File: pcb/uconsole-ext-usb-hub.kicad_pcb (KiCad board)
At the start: 2 copper layers, 32.1 x 77 mm, 38 parts, among them J1 MINI_PCIE, J2 SPEAKER, J3 SPEAKER, P1 USB_C_Plug_USB2.0, P2 USB_C_Plug_USB2.0, P3 USB_C_Plug_USB2.0, P4 USB_C_Plug_USB2.0, U1 TUSB2048B, U2 TPS2044D, U3 USBLC6-2P6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

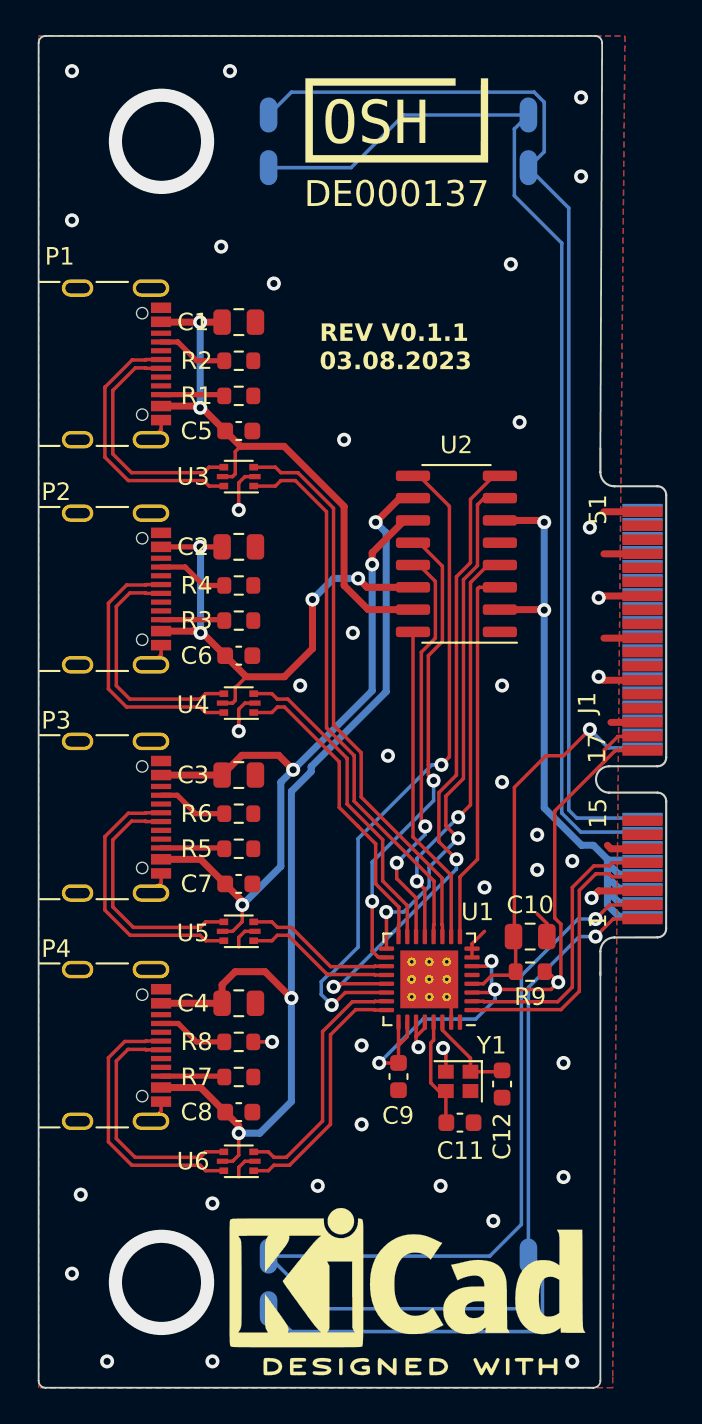
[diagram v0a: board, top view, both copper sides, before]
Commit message: Some updates of sch, pcb and readme
* Add 3 u.fl connectors for antennas
* Update pictures in readme

Signed-off-by: argz <kirill.snezhko@pm.me>
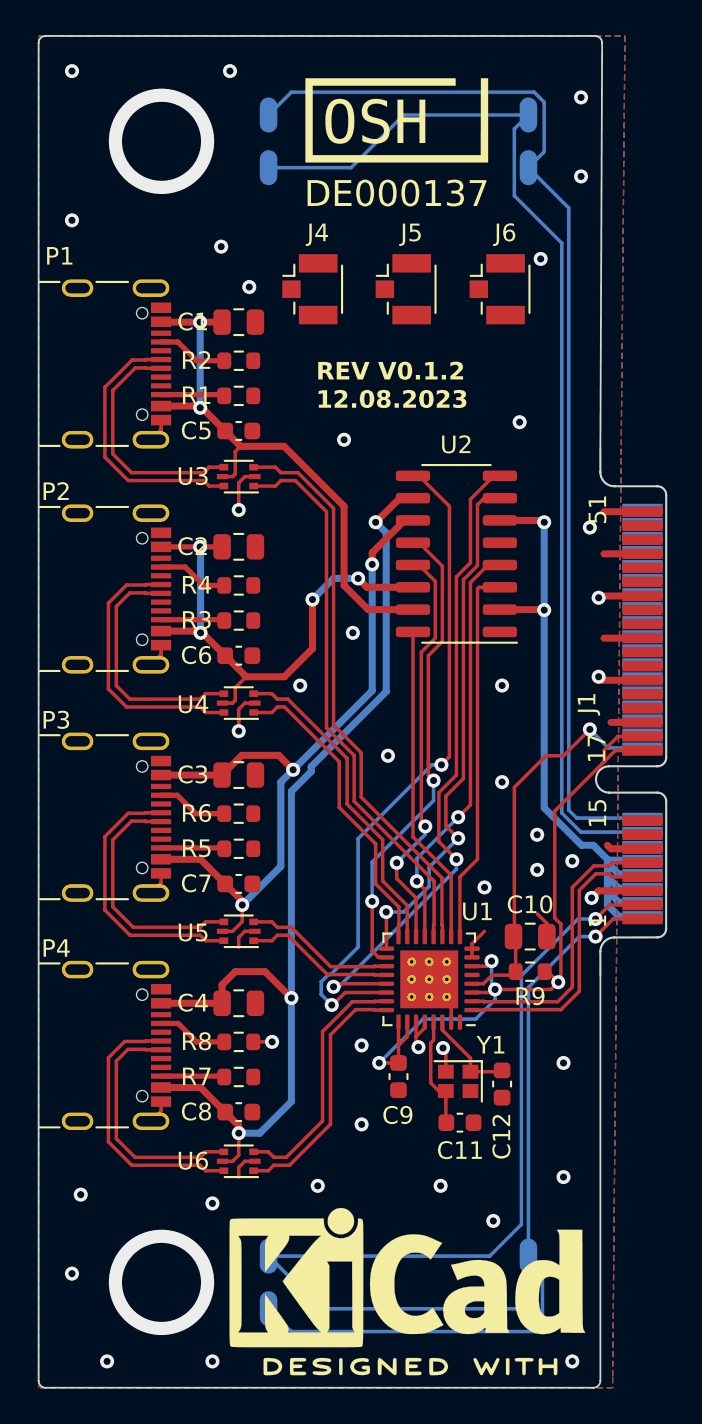
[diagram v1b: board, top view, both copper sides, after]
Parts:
- added J4: MAIN, Connector_Coaxial:U.FL_Hirose_U.FL-R-SMT-1_Vertical, F.Cu at (151.1, 75.9)
- added J5: AUX, Connector_Coaxial:U.FL_Hirose_U.FL-R-SMT-1_Vertical, F.Cu at (156.4, 75.9)
- added J6: GPS, Connector_Coaxial:U.FL_Hirose_U.FL-R-SMT-1_Vertical, F.Cu at (161.7, 75.9)
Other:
- outline, holes or cut-outs redrawn
- board text added: "REV V0.1.2 12.08.2023"
- board text removed: "REV V0.1.1 03.08.2023"
